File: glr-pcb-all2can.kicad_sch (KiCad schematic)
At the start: 30 parts, among them IC2 ZMR330FTA, IC3 AP64060WU-7, IC4 STM32C092KCT6, J1 DA15_Pins_MountingHoles, J2 Conn_02x04_Top_Bottom, J3 Conn_01x04, J4 Conn_01x02, J5 Conn_01x02

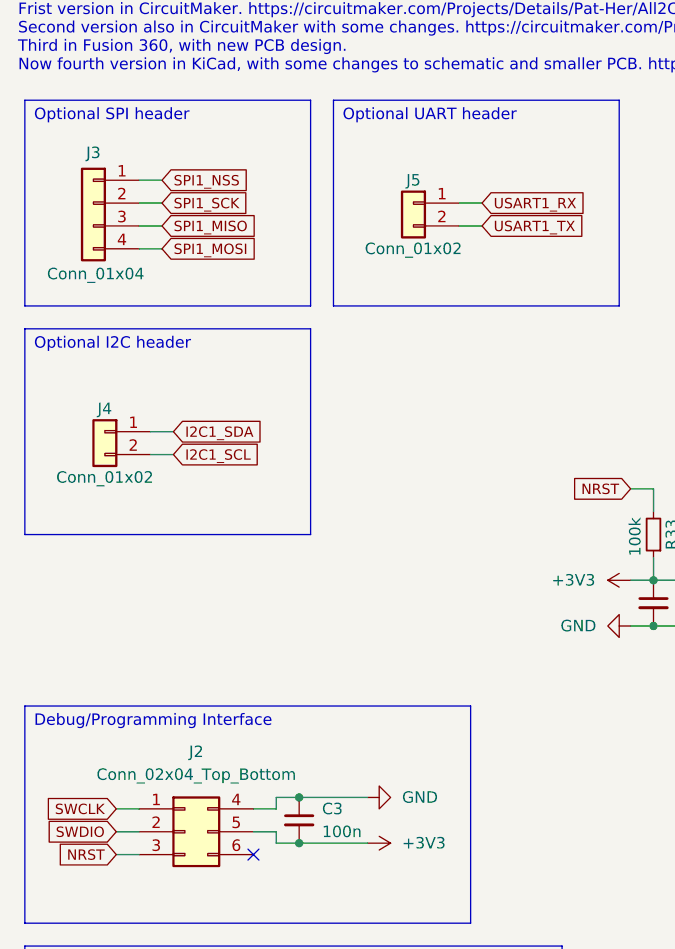
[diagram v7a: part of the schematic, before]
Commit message: group parts on pcb
replace footprints
update can setup
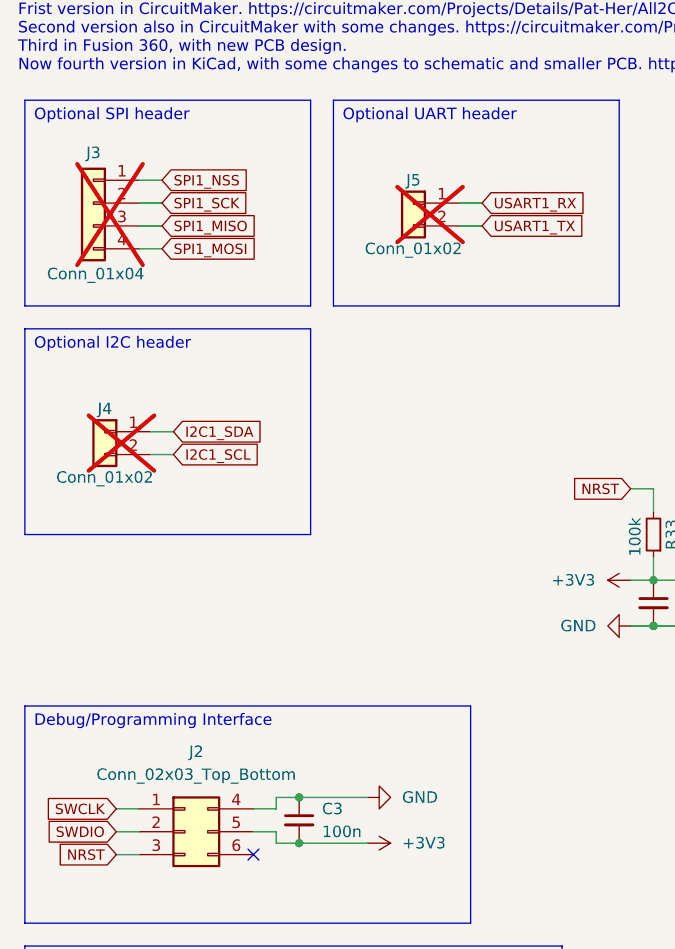
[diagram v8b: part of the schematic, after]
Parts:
- C15, C16, C17, C18, C19, C20, C21, C23, C24, C3, C4, C6: footprint (none) -> Capacitor_SMD:C_0603_1608Metric
- D1, D2: footprint (none) -> LED_SMD:LED_0603_1608Metric
- IC2: footprint ZMR330FTA -> SamacSys_Parts:ZMR330FTA
- IC3: footprint SOT95P280X100-6N -> SamacSys_Parts:SOT95P280X100-6N
- IC4: footprint QFP80P900X900X160-32N -> SamacSys_Parts:QFP80P900X900X160-32N
- J2: value Conn_02x04_Top_Bottom -> Conn_02x03_Top_Bottom; footprint Connector_PinSocket_2.54mm:PinSocket_2x03_P2.54mm_Vertical -> Connector_PinHeader_2.54mm:PinHeader_2x03_P2.54mm_Vertical
- J3: footprint Connector_PinSocket_2.54mm:PinSocket_1x04_P2.54mm_Vertical -> Connector_PinHeader_2.54mm:PinHeader_1x04_P2.54mm_Vertical; now not fitted; now left out of the parts list
- J4, J5: footprint Connector_PinSocket_2.54mm:PinSocket_1x04_P2.54mm_Vertical -> Connector_PinHeader_2.54mm:PinHeader_1x02_P2.54mm_Vertical; now not fitted; now left out of the parts list
- L1: footprint (none) -> Inductor_SMD:L_1008_2520Metric
- R29, R3, R30, R31, R32, R33, R4: footprint (none) -> Resistor_SMD:R_0603_1608Metric
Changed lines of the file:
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@@
 		)
 	)
-	(global_label "LED_2"
+	(global_label "LED_1"
 		(shape input)
-		(at 110.49 151.13 0)
+		(at 110.49 140.97 0)
 		(fields_autoplaced yes)
 		(effects
@@
 		)
 		(property "Intersheetrefs" "${INTERSHEET_REFS}"
-			(at 118.2384 151.13 0)
+			(at 118.2384 140.97 0)
 			(effects
 				(font
@@
 		)
 	)
-	(global_label "LED_1"
+	(global_label "LED_2"
 		(shape input)
-		(at 110.49 140.97 0)
+		(at 110.49 151.13 0)
 		(fields_autoplaced yes)
 		(effects
@@
 		)
 		(property "Intersheetrefs" "${INTERSHEET_REFS}"
-			(at 118.2384 140.97 0)
+			(at 118.2384 151.13 0)
 			(effects
 				(font
@@
 		)
 	)
-	(global_label "IC_OUT_3"
+	(global_label "IC_OUT_2"
 		(shape input)
-		(at 128.27 50.8 90)
+		(at 130.81 50.8 90)
 		(fields_autoplaced yes)
 		(effects
@@
 		)
 		(property "Intersheetrefs" "${INTERSHEET_REFS}"
-			(at 128.27 40.3301 90)
+			(at 130.81 40.3301 90)
 			(effects
 				(font
@@
 		)
 	)
-	(global_label "IC_OUT_2"
+	(global_label "IC_OUT_3"
 		(shape input)
-		(at 130.81 50.8 90)
+		(at 128.27 50.8 90)
 		(fields_autoplaced yes)
 		(effects
@@
 		)
 		(property "Intersheetrefs" "${INTERSHEET_REFS}"
-			(at 130.81 40.3301 90)
+			(at 128.27 40.3301 90)
 			(effects
 				(font
@@
 			)
 		)
-		(property "Footprint" ""
+		(property "Footprint" "Capacitor_SMD:C_0603_1608Metric"
 			(at 85.09 83.82 0)
 			(effects
@@
 			)
 		)
-		(property "Footprint" ""
+		(property "Footprint" "Resistor_SMD:R_0603_1608Metric"
 			(at 95.25 172.72 0)
 			(effects
@@
 			)
 		)
-		(property "Footprint" ""
+		(property "Footprint" "Capacitor_SMD:C_0603_1608Metric"
 			(at 59.69 132.08 0)
 			(effects
@@
 			)
 		)
-		(property "Footprint" ""
+		(property "Footprint" "Resistor_SMD:R_0603_1608Metric"
 			(at 66.04 182.88 0)
 			(effects
@@
 			)
 		)
-		(property "Footprint" ""
+		(property "Footprint" "LED_SMD:LED_0603_1608Metric"
 			(at 104.14 151.13 0)
 			(effects
@@
 			)
 		)
-		(property "Value" "Conn_02x04_Top_Bottom"
+		(property "Value" "Conn_02x03_Top_Bottom"
 			(at 34.29 102.87 0)
 			(effects
@@
 			)
 		)
-		(property "Footprint" "Connector_PinSocket_2.54mm:PinSocket_2x03_P2.54mm_Vertical"
+		(property "Footprint" "Connector_PinHeader_2.54mm:PinHeader_2x03_P2.54mm_Vertical"
 			(at 33.02 109.22 0)
 			(effects
@@
 			)
 		)
-		(property "Footprint" "QFP80P900X900X160-32N"
+		(property "Footprint" "SamacSys_Parts:QFP80P900X900X160-32N"
 			(at 147.32 155.88 0)
 			(effects
@@
 			)
 		)
-		(property "Footprint" ""
+		(property "Footprint" "Capacitor_SMD:C_0603_1608Metric"
 			(at 140.97 40.64 0)
 			(effects
@@
 			)
 		)
-		(property "Footprint" ""
+		(property "Footprint" "Capacitor_SMD:C_0603_1608Metric"
 			(at 67.31 172.72 0)
 			(effects
@@
 			)
 		)
-		(property "Footprint" "ZMR330FTA"
+		(property "Footprint" "SamacSys_Parts:ZMR330FTA"
 			(at 25.4 232.08 0)
 			(effects
@@
 			)
 		)
-		(property "Footprint" ""
+		(property "Footprint" "Resistor_SMD:R_0603_1608Metric"
 			(at 135.89 45.72 0)
 			(effects
@@
 			)
 		)
-		(property "Footprint" ""
+		(property "Footprint" "LED_SMD:LED_0603_1608Metric"
 			(at 104.14 140.97 0)
 			(effects
@@
 			)
 		)
-		(property "Footprint" ""
+		(property "Footprint" "Resistor_SMD:R_0603_1608Metric"
 			(at 101.6 167.64 0)
 			(effects
@@
 			)
 		)
-		(property "Footprint" ""
+		(property "Footprint" "Capacitor_SMD:C_0603_1608Metric"
 			(at 80.01 185.42 0)
 			(effects
@@
 			)
 		)
-		(property "Footprint" ""
+		(property "Footprint" "Capacitor_SMD:C_0603_1608Metric"
 			(at 90.17 185.42 0)
 			(effects
@@
 			)
 		)
-		(property "Footprint" ""
+		(property "Footprint" "Resistor_SMD:R_0603_1608Metric"
 			(at 95.25 151.13 0)
 			(effects
@@
 			)
 		)
-		(property "Footprint" ""
+		(property "Footprint" "Capacitor_SMD:C_0603_1608Metric"
 			(at 123.19 172.72 0)
 			(effects
@@
 		(unit 1)
 		(exclude_from_sim no)
-		(in_bom yes)
+		(in_bom no)
 		(on_board yes)
-		(dnp no)
+		(dnp yes)
 		(property "Reference" "J4"
 			(at 24.13 62.23 0)
@@
 			)
 		)
-		(property "Footprint" "Connector_PinSocket_2.54mm:PinSocket_1x04_P2.54mm_Vertical"
+		(property "Footprint" "Connector_PinHeader_2.54mm:PinHeader_1x02_P2.54mm_Vertical"
 			(at 24.13 64.77 0)
 			(effects
@@
 			)
 		)
-		(property "Footprint" ""
+		(property "Footprint" "Capacitor_SMD:C_0603_1608Metric"
 			(at 83.82 172.72 0)
 			(effects
@@
 		(unit 1)
 		(exclude_from_sim no)
-		(in_bom yes)
+		(in_bom no)
 		(on_board yes)
-		(dnp no)
+		(dnp yes)
 		(property "Reference" "J5"
 			(at 58.42 36.83 0)
@@
 			)
 		)
-		(property "Footprint" "Connector_PinSocket_2.54mm:PinSocket_1x04_P2.54mm_Vertical"
+		(property "Footprint" "Connector_PinHeader_2.54mm:PinHeader_1x02_P2.54mm_Vertical"
 			(at 58.42 39.37 0)
 			(effects
@@
 			)
 		)
-		(property "Footprint" ""
+		(property "Footprint" "Capacitor_SMD:C_0603_1608Metric"
 			(at 45.72 107.95 0)
 			(effects
@@
 			)
 		)
-		(property "Footprint" ""
+		(property "Footprint" "Capacitor_SMD:C_0603_1608Metric"
 			(at 59.69 144.78 0)
 			(effects
@@
 			)
 		)
-		(property "Footprint" ""
+		(property "Footprint" "Inductor_SMD:L_1008_2520Metric"
 			(at 72.39 177.8 0)
 			(effects
@@
 			)
 		)
-		(property "Datasheet" "~"
+		(property "Datasheet" "https://www.we-online.com/components/products/datasheet/74479889310.pdf"
 			(at 72.39 177.8 0)
 			(effects
@@
 			)
 		)
-		(property "Footprint" ""
+		(property "Footprint" "Resistor_SMD:R_0603_1608Metric"
 			(at 95.25 140.97 0)
 			(effects
@@
 		(unit 1)
 		(exclude_from_sim no)
-		(in_bom yes)
+		(in_bom no)
 		(on_board yes)
-		(dnp no)
+		(dnp yes)
 		(property "Reference" "J3"
 			(at 22.86 33.782 0)
@@
 			)
 		)
-		(property "Footprint" "Connector_PinSocket_2.54mm:PinSocket_1x04_P2.54mm_Vertical"
+		(property "Footprint" "Connector_PinHeader_2.54mm:PinHeader_1x04_P2.54mm_Vertical"
 			(at 22.86 39.37 0)
 			(effects
@@
 			)
 		)
-		(property "Footprint" ""
+		(property "Footprint" "Capacitor_SMD:C_0603_1608Metric"
 			(at 113.03 172.72 0)
 			(effects
@@
 			)
 		)
-		(property "Footprint" "SOT95P280X100-6N"
+		(property "Footprint" "SamacSys_Parts:SOT95P280X100-6N"
 			(at 57.15 272.72 0)
 			(effects
@@
 			)
 		)
-		(property "Footprint" ""
+		(property "Footprint" "Resistor_SMD:R_0603_1608Metric"
 			(at 85.09 76.2 0)
 			(effects
@@
 			)
 		)
-		(property "Footprint" ""
+		(property "Footprint" "Capacitor_SMD:C_0603_1608Metric"
 			(at 49.53 144.78 0)
 			(effects
